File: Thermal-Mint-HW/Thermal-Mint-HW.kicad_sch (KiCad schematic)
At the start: 0 parts

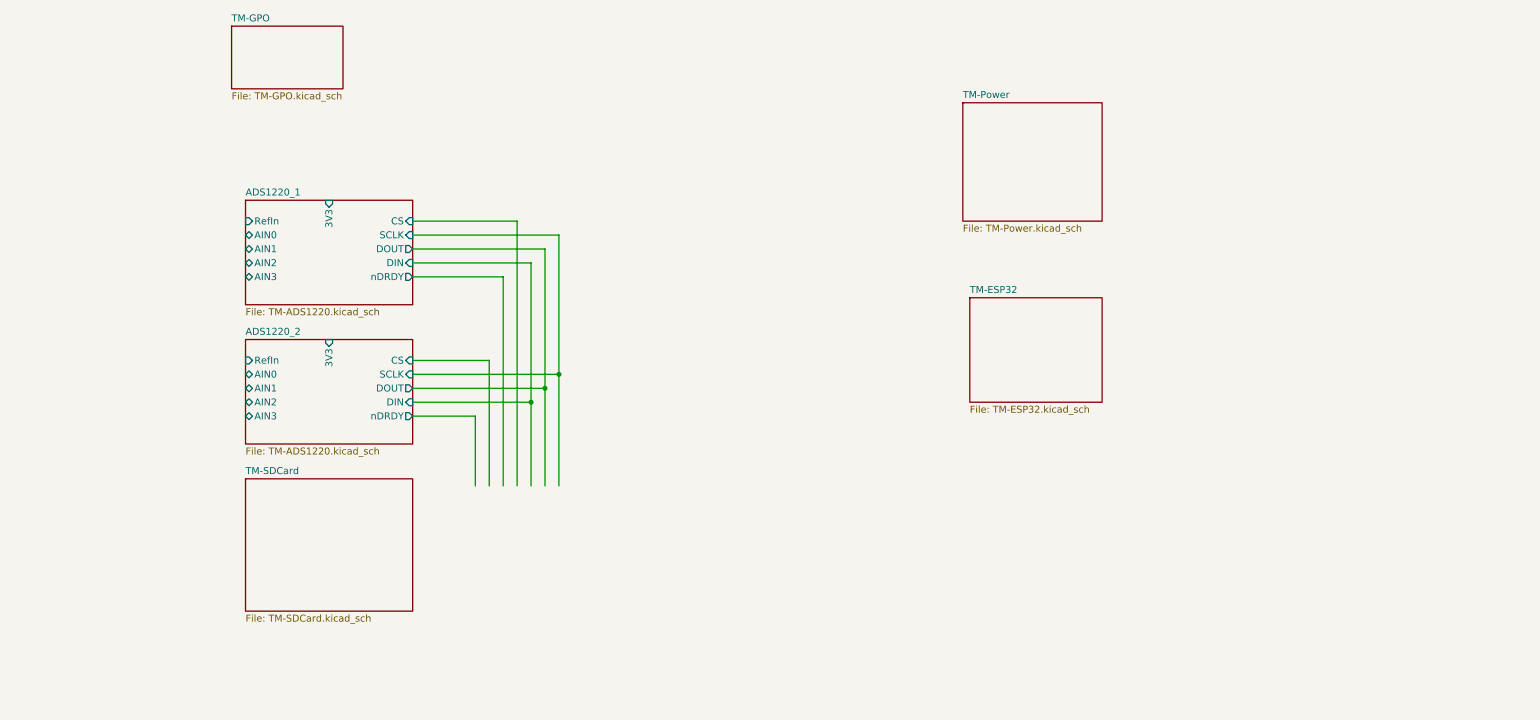
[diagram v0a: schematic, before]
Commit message: WIP commit, Adding connectors and memory
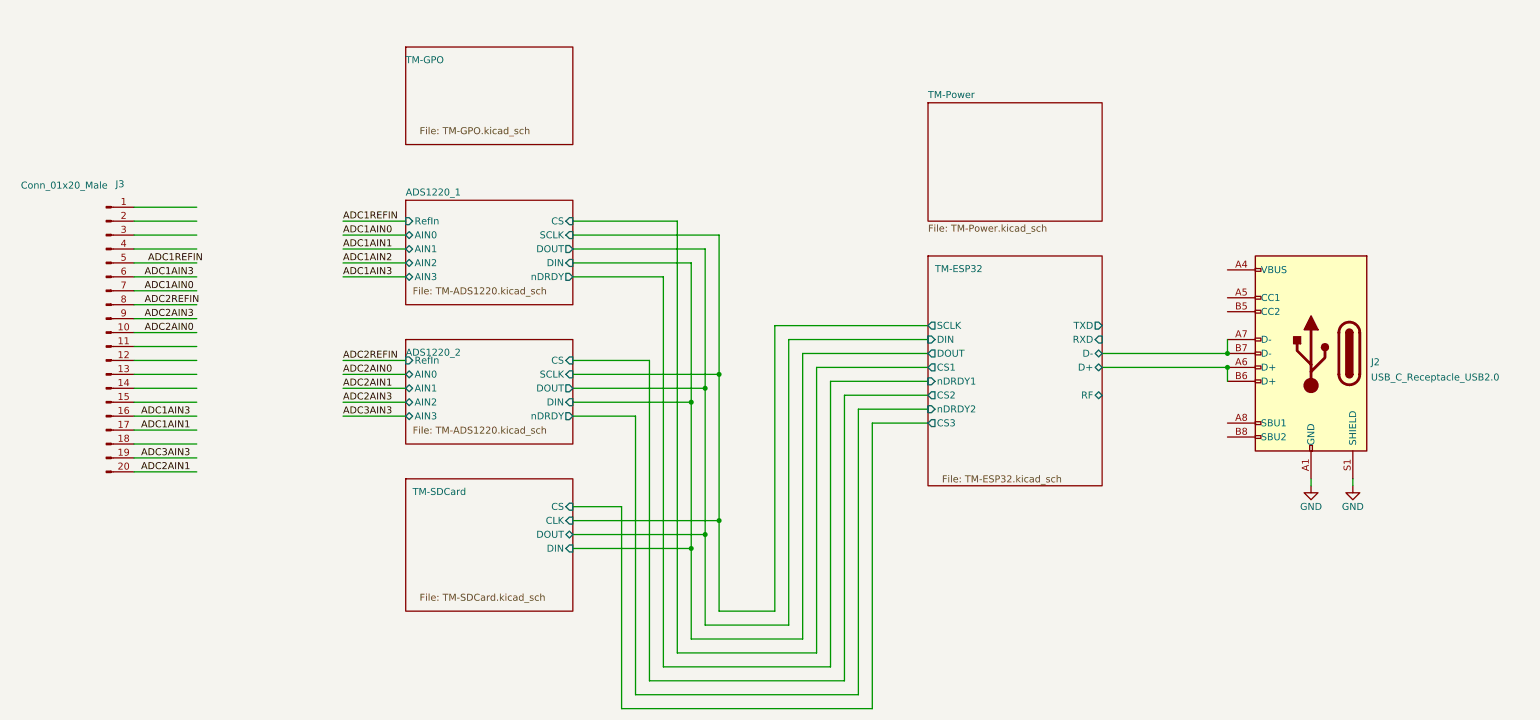
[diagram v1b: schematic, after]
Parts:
- added J2: USB_C_Receptacle_USB2.0, ThermalMint:USB4110-GF-A, symbol Connector:USB_C_Receptacle_USB2.0
- added J3: Conn_01x20_Male, ThermalMint:1786918_02_DMC, symbol Connector:Conn_01x20_Male
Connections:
- new net: J2.A4 (VBUS), J2.A9 (VBUS), J2.B4 (VBUS), J2.B9 (VBUS)
- new net ADC1AIN0: J3.7 (Pin_7)
- new net ADC1AIN1: J3.17 (Pin_17)
- new net ADC1AIN3: J3.16 (Pin_16), J3.6 (Pin_6)
- new net ADC1REFIN: J3.5 (Pin_5)
- new net ADC2AIN0: J3.10 (Pin_10)
- new net ADC2AIN1: J3.20 (Pin_20)
- new net ADC2AIN3: J3.9 (Pin_9)
- new net ADC2REFIN: J3.8 (Pin_8)
- new net ADC3AIN3: J3.19 (Pin_19)
- new net GND: J2.A1 (GND), J2.A12 (GND), J2.B1 (GND), J2.B12 (GND), J2.S1 (SHIELD)
- new net TM-ESP32/D+: J2.A6 (D+), J2.B6 (D+)
- new net TM-ESP32/D-: J2.A7 (D-), J2.B7 (D-)
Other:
- sheet ADS1220_1 ports: added none; removed 3V3
- sheet ADS1220_2 ports: added none; removed 3V3
- sheet TM-ESP32 ports: added CS1, CS2, CS3, D+, D-, DIN, DOUT, RF, RXD, SCLK, TXD, nDRDY1, nDRDY2; removed none
- sheet TM-SDCard ports: added CLK, CS, DIN, DOUT; removed none

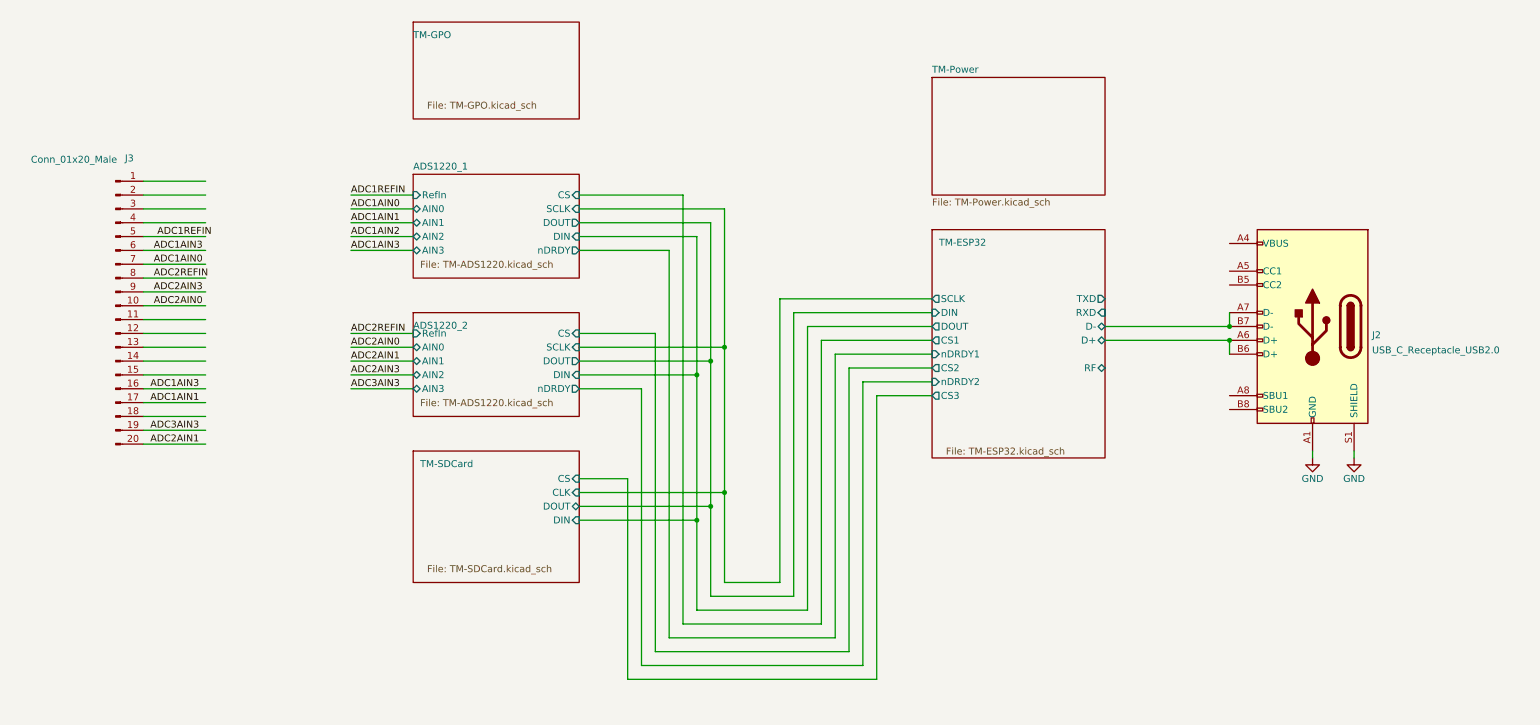
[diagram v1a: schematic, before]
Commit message: Clean up of output circuits
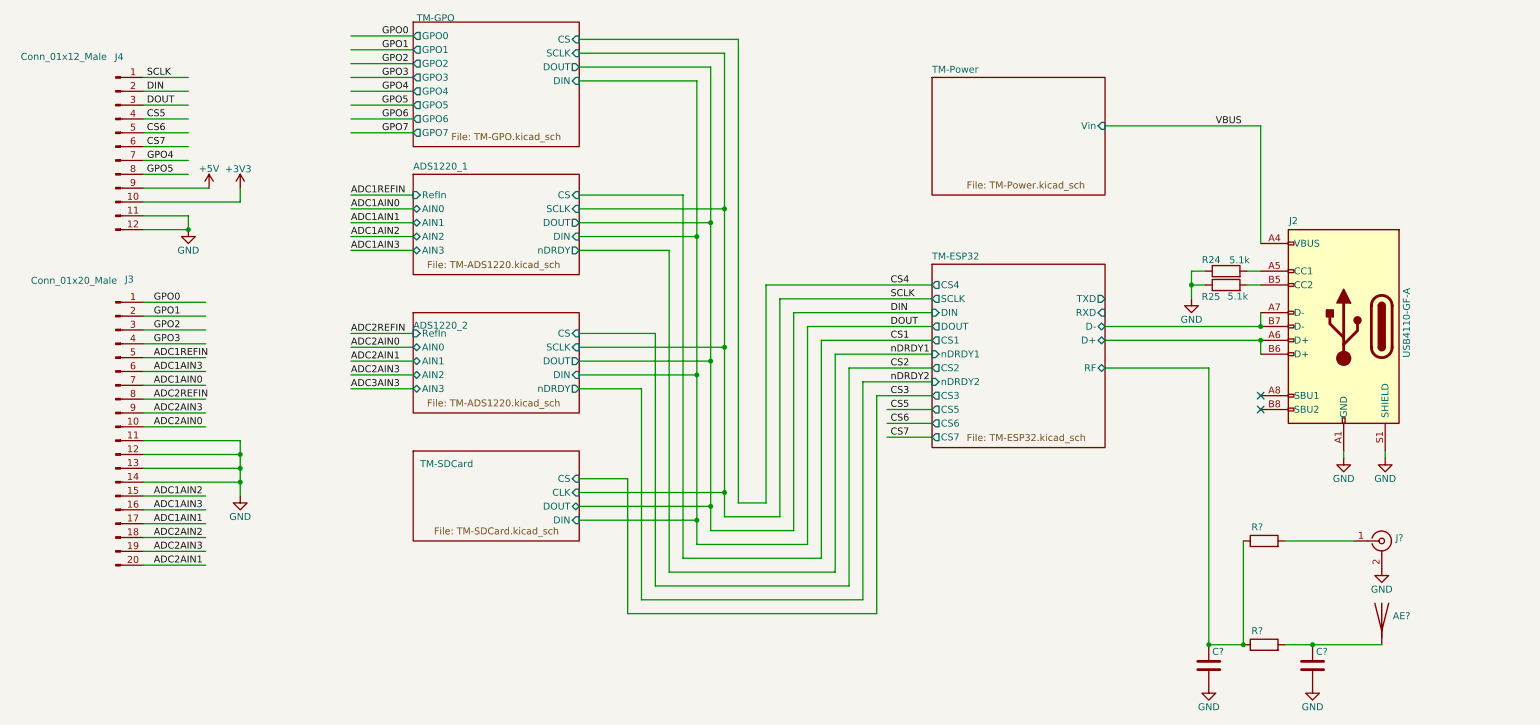
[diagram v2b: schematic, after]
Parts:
- added AE?: (no value), symbol Device:Antenna
- added C? (x2): (no value), Capacitor_SMD:C_0603_1608Metric_Pad1.08x0.95mm_HandSolder, symbol Device:C
- added J4: Conn_01x12_Male, Connector_PinHeader_2.54mm:PinHeader_2x05_P2.54mm_Vertical, symbol Connector:Conn_01x12_Male
- added J?: (no value), symbol Connector:Conn_Coaxial
- added R24, R25: 5.1k, Resistor_SMD:R_0603_1608Metric_Pad0.98x0.95mm_HandSolder, symbol Device:R
- added R? (x2): (no value), Resistor_SMD:R_0603_1608Metric_Pad0.98x0.95mm_HandSolder, symbol Device:R
- J2: value USB_C_Receptacle_USB2.0 -> USB4110-GF-A
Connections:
- net ADC1AIN2: now also J3.15 (Pin_15)
- net ADC2AIN3: now also J3.19 (Pin_19)
- net ADC3AIN3: no longer J3.19 (Pin_19)
- net GND: now also J3.11 (Pin_11), J3.12 (Pin_12), J3.13 (Pin_13), J3.14 (Pin_14), C?.2, C?.2, J4.11 (Pin_11), J4.12 (Pin_12), J?.2 (Ext), R24.1, R25.1
- net TM-ESP32/RF: now also C?.1, R?.1, R?.1
- net VBUS: now reaches J2.A4 (VBUS), J2.A9 (VBUS), J2.B4 (VBUS), J2.B9 (VBUS)
- net at J2.A5 (CC1): now also R24.2
- net at J2.B5 (CC2): now also R25.2
- net GPO0: now reaches J3.1 (Pin_1)
- net ADC2AIN2: now reaches J3.18 (Pin_18)
- net GPO1: now reaches J3.2 (Pin_2)
- net GPO2: now reaches J3.3 (Pin_3)
- net GPO3: now reaches J3.4 (Pin_4)
- new net: AE?.1 (A), C?.1, R?.2
- new net: J?.1 (In), R?.2
- new net +3V3: J4.10 (Pin_10)
- new net +5V: J4.9 (Pin_9)
- new net CS5: J4.4 (Pin_4)
- new net CS6: J4.5 (Pin_5)
- new net CS7: J4.6 (Pin_6)
- new net DIN: J4.2 (Pin_2)
- new net DOUT: J4.3 (Pin_3)
- new net GPO4: J4.7 (Pin_7)
- new net GPO5: J4.8 (Pin_8)
- new net SCLK: J4.1 (Pin_1)
- no-connect marks 0 -> 2
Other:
- sheet TM-ESP32 ports: added CS4, CS5, CS6, CS7; removed none
- sheet TM-GPO ports: added CS, DIN, DOUT, GPO0, GPO1, GPO2, GPO3, GPO4, GPO5, GPO6, GPO7, SCLK; removed none
- sheet TM-Power ports: added Vin; removed none
- moved on the sheet: J2, J3

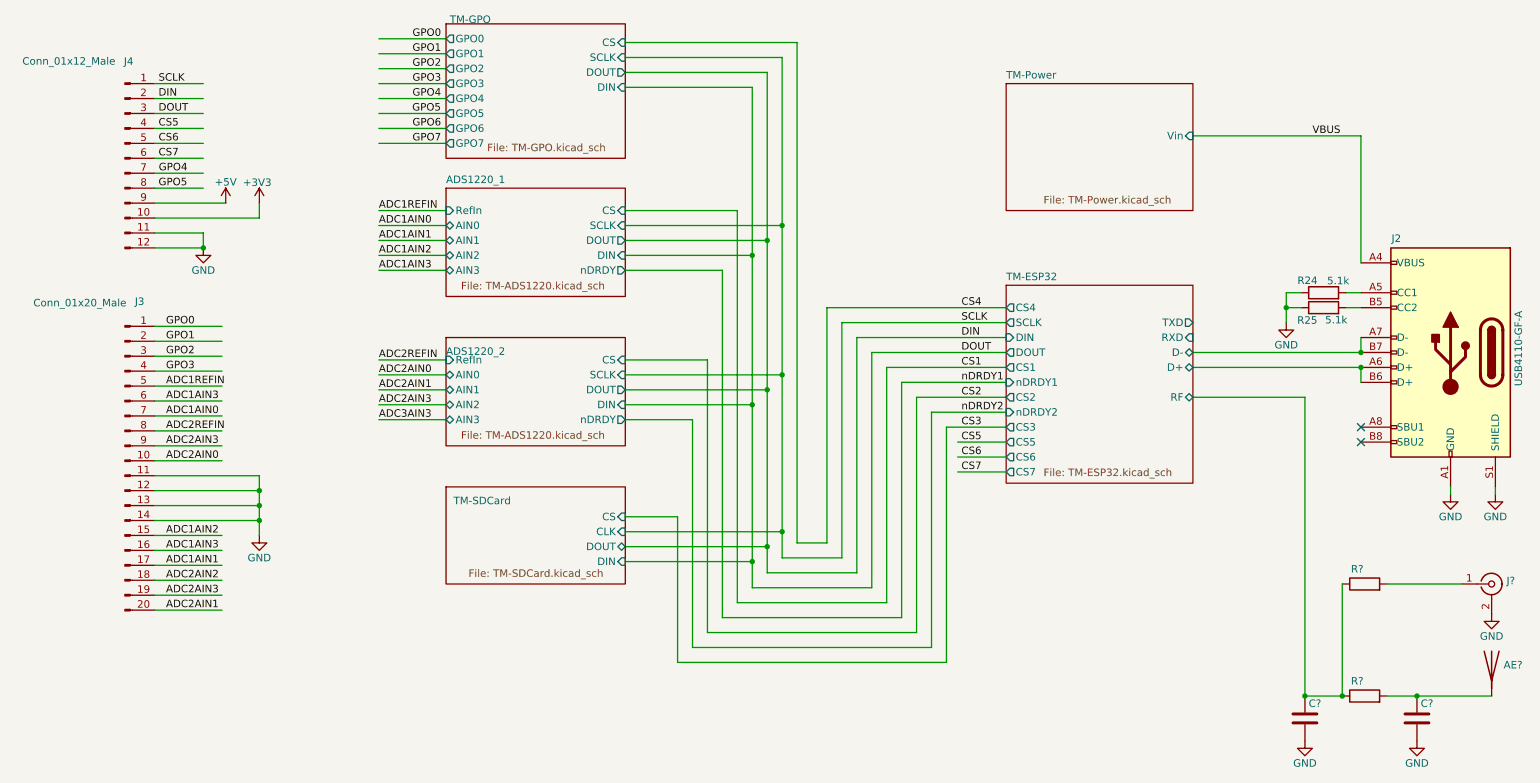
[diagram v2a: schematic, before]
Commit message: Cleanup of Rev1 schematics for review
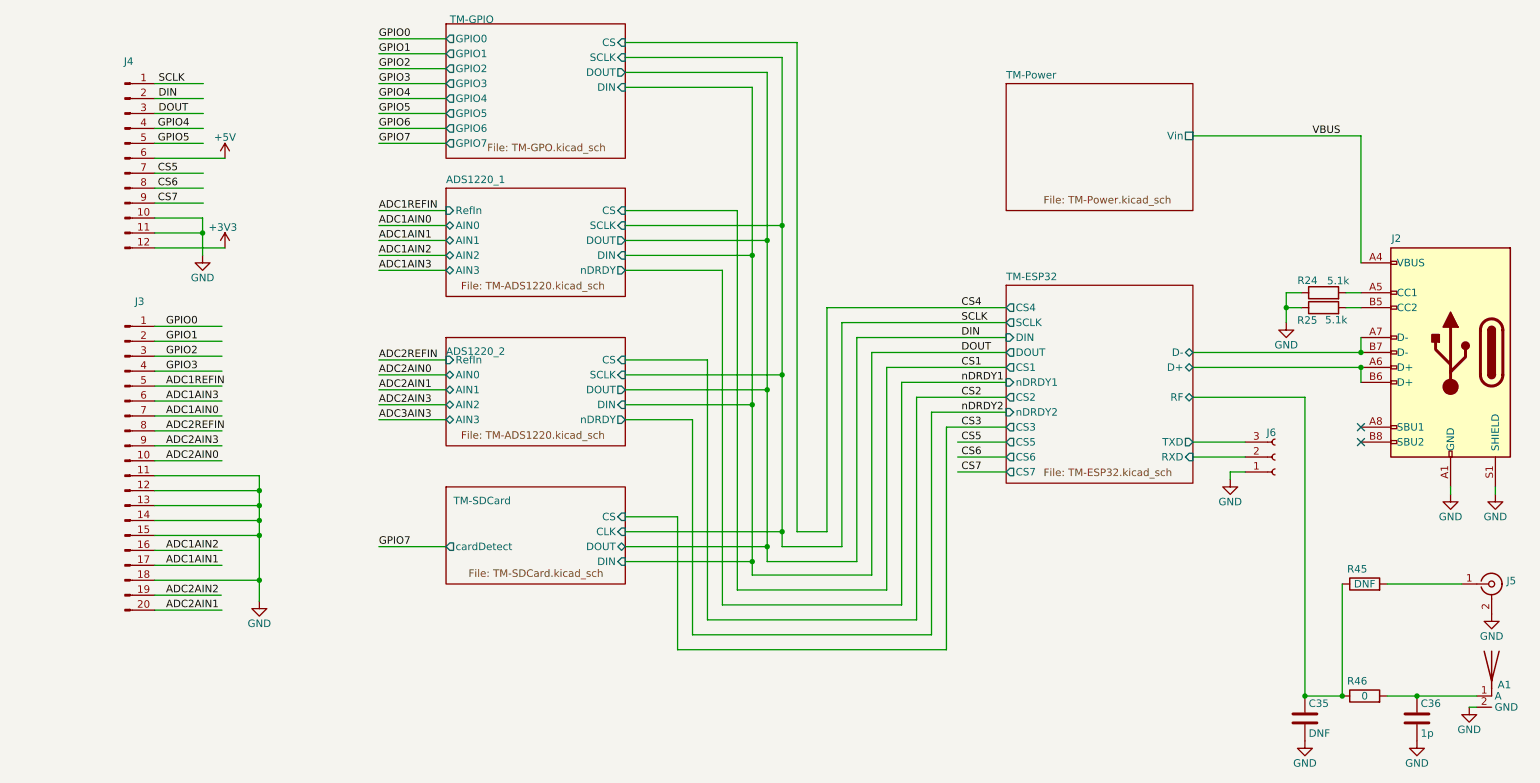
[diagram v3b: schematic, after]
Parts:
- removed AE?: (no value), symbol Device:Antenna
- added A1: (no value), symbol ThermalMint:AntennaWithGround
- added J6: (no value), symbol Connector:Conn_01x03_Female
- C35: renamed from C?; value (none) -> DNF
- C36: renamed from C?; value (none) -> 1p
- J2: value USB4110-GF-A -> (none); footprint ThermalMint:USB4110-GF-A -> (none)
- J3: value Conn_01x20_Male -> (none)
- J4: value Conn_01x12_Male -> (none); footprint Connector_PinHeader_2.54mm:PinHeader_2x05_P2.54mm_Vertical -> (none)
- R45: renamed from R?; value (none) -> DNF
- R46: renamed from R?; value (none) -> 0
- gave numbers to parts that had none: 1
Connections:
- net GPO4 is gone; now on net CS5: J4.7 (Pin_7)
- net GPO5 is gone; now on net CS6: J4.8 (Pin_8)
- net +3V3: now also J4.12 (Pin_12); no longer J4.10 (Pin_10)
- net +5V: now also J4.6 (Pin_6); no longer J4.9 (Pin_9)
- net ADC1AIN2: now also J3.16 (Pin_16); no longer J3.15 (Pin_15)
- net ADC1AIN3: no longer J3.16 (Pin_16)
- net ADC2AIN2: now also J3.19 (Pin_19); no longer J3.18 (Pin_18)
- net ADC2AIN3: no longer J3.19 (Pin_19)
- net CS5: no longer J4.4 (Pin_4)
- net CS6: no longer J4.5 (Pin_5)
- net CS7: now also J4.9 (Pin_9); no longer J4.6 (Pin_6)
- net GND: now also J3.15 (Pin_15), J3.18 (Pin_18), J4.10 (Pin_10), A1.2 (GND), J6.1 (Pin_1); no longer J4.12 (Pin_12)
- net TM-ESP32/RXD: now also J6.2 (Pin_2)
- net TM-ESP32/TXD: now also J6.3 (Pin_3)
- net at C36.1, R46.2: now also A1.1 (A)
- net GPO0 renamed GPIO0
- net GPO1 renamed GPIO1
- net GPO2 renamed GPIO2
- net GPO3 renamed GPIO3
- new net GPIO4: J4.4 (Pin_4)
- new net GPIO5: J4.5 (Pin_5)
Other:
- sheet TM-GPO renamed TM-GPIO
- sheet TM-GPIO ports: added GPIO0, GPIO1, GPIO2, GPIO3, GPIO4, GPIO5, GPIO6, GPIO7; removed GPO0, GPO1, GPO2, GPO3, GPO4, GPO5, GPO6, GPO7
- sheet TM-SDCard ports: added cardDetect; removed none
